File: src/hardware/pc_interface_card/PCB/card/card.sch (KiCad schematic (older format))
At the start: 16 parts, among them J1 USBC_IO_PWR, J2 USBC_PWR_ONLY, J3 10018784-10201TLF, J4 PD_I2C

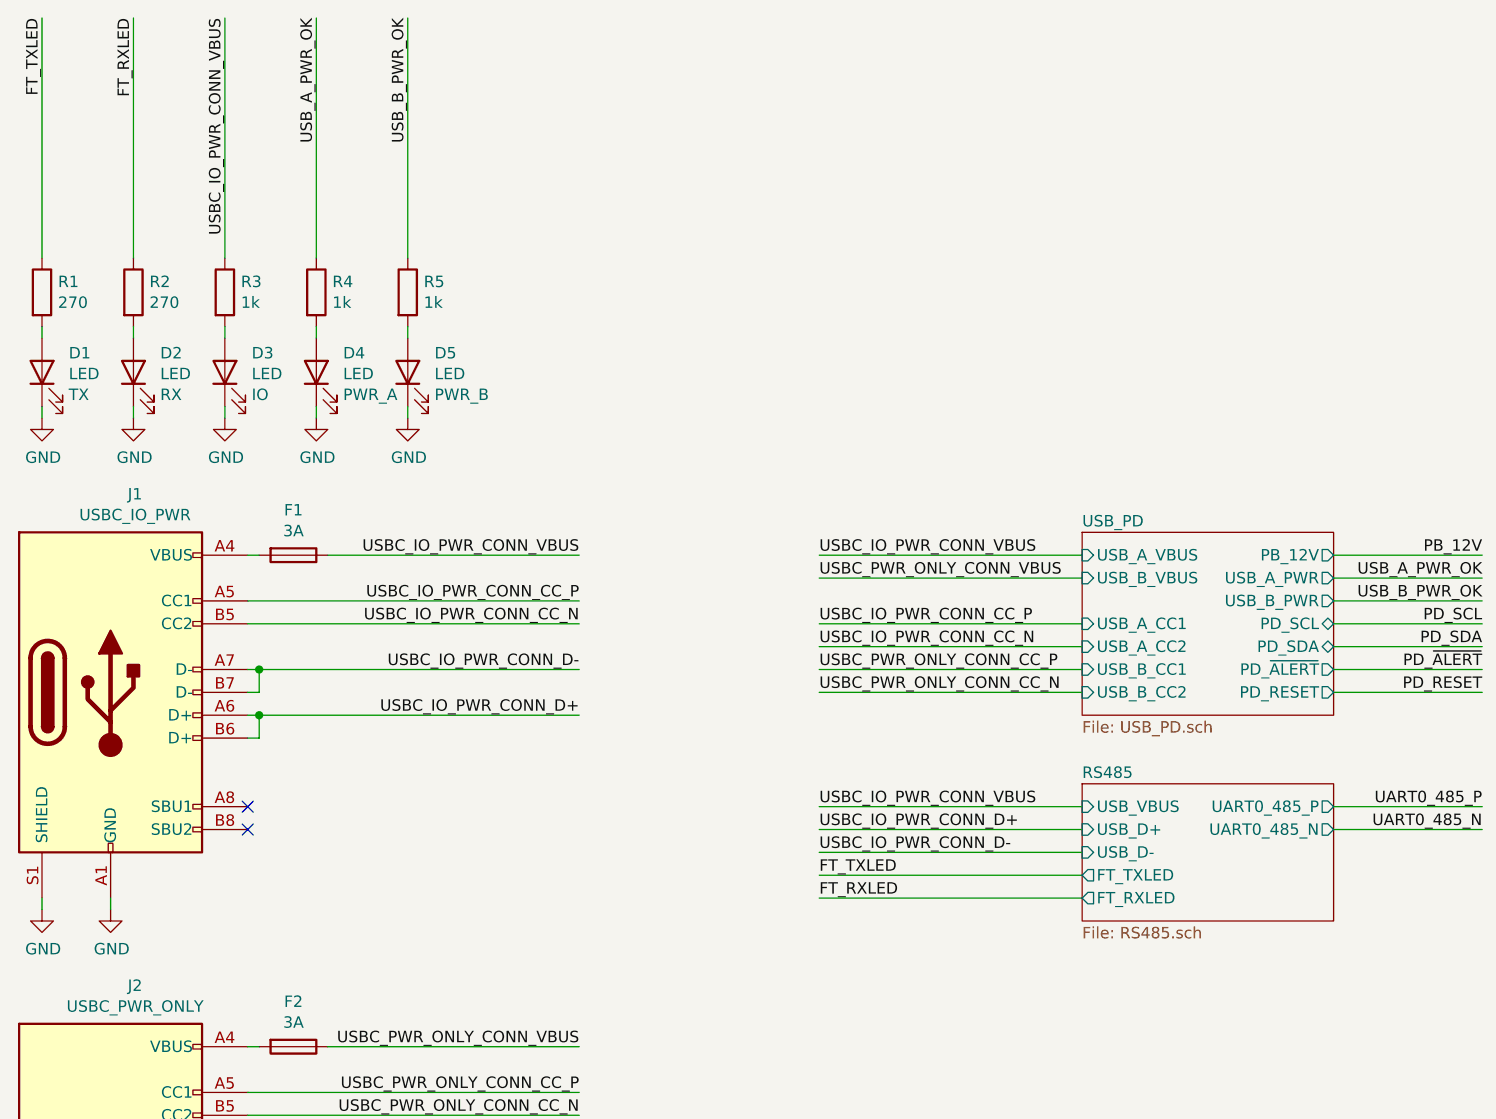
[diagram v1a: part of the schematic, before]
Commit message: Fixing RXLED and TXLED polarization
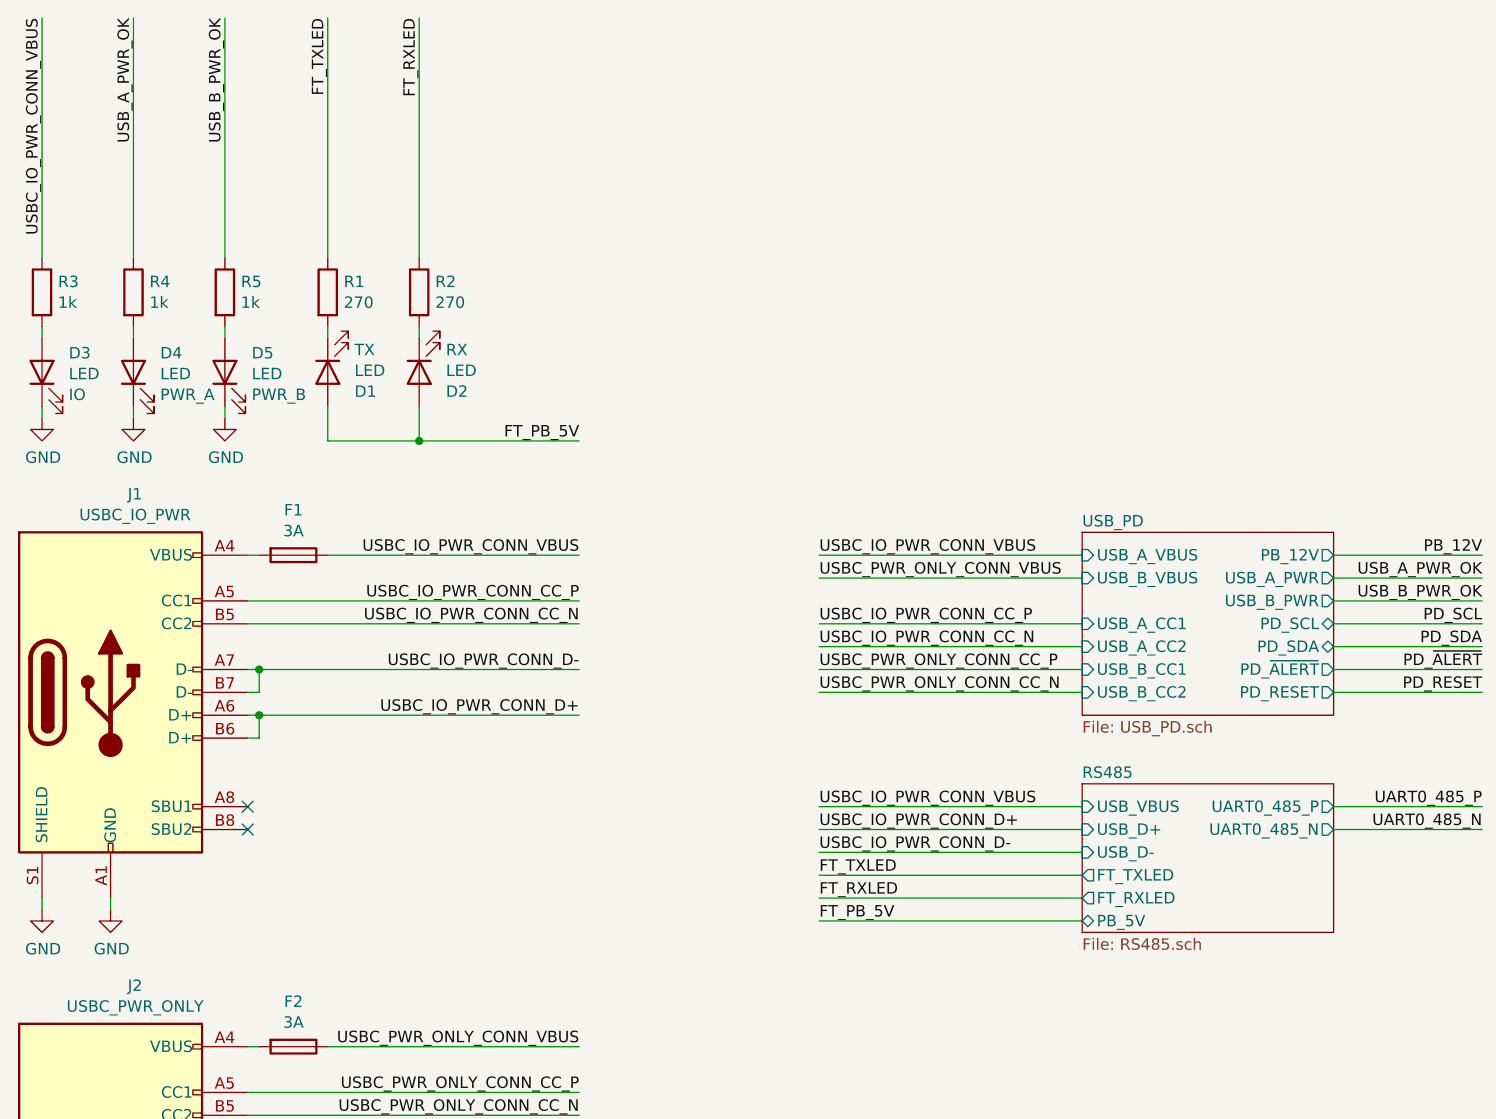
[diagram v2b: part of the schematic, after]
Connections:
- net GND: no longer D1.1 (K), D2.1 (K)
- net at R1.2: now also D1.1 (K); no longer D1.2 (A)
- net at R2.2: now also D2.1 (K); no longer D2.2 (A)
- new net FT_PB_5V: D1.2 (A), D2.2 (A)
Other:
- moved on the sheet: D1, D2, D3, D4, D5, R1, R2, R3, R4, R5
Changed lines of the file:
@@
 	8100 1850 8650 1850
-$Comp
-L Device:LED D1
-U 1 1 5E969A63
-P 1000 2150
-F 0 "D1" V 1084 2033 50  0000 R CNN
-F 1 "LED" V 993 2033 50  0000 R CNN
-F 2 "LED_THT:LED_D3.0mm" H 1000 2150 50  0001 C CNN
-F 3 "~" H 1000 2150 50  0001 C CNN
-F 4 "TX" V 902 2033 50  0000 R CNN "Info"
-	1    1000 2150
-	0    -1   -1   0
-$EndComp
 $Comp
 L Device:R R1
 U 1 1 5E96B671
-P 1000 1800
-F 0 "R1" H 1070 1846 50  0000 L CNN
-F 1 "270" H 1070 1755 50  0000 L CNN
-F 2 "Resistor_SMD:R_0603_1608Metric" V 930 1800 50  0001 C CNN
-F 3 "~" H 1000 1800 50  0001 C CNN
-	1    1000 1800
-	1    0    0    -1
-$EndComp
-$Comp
-L power:GND #PWR01
-U 1 1 5E970CD5
-P 1000 2350
-F 0 "#PWR01" H 1000 2100 50  0001 C CNN
-F 1 "GND" H 1005 2177 50  0000 C CNN
-F 2 "" H 1000 2350 50  0001 C CNN
-F 3 "" H 1000 2350 50  0001 C CNN
-	1    1000 2350
-	1    0    0    -1
-$EndComp
-Wire Wire Line
-	1000 2300 1000 2350
-Wire Wire Line
-	1000 1950 1000 2000
+P 2250 1800
+F 0 "R1" H 2320 1846 50  0000 L CNN
+F 1 "270" H 2320 1755 50  0000 L CNN
+F 2 "Resistor_SMD:R_0603_1608Metric" V 2180 1800 50  0001 C CNN
+F 3 "~" H 2250 1800 50  0001 C CNN
+	1    2250 1800
+	1    0    0    -1
+$EndComp
+Wire Wire Line
+	2250 1950 2250 2000
 $Comp
 L Device:LED D2
 U 1 1 5E97516D
-P 1400 2150
-F 0 "D2" V 1484 2033 50  0000 R CNN
-F 1 "LED" V 1393 2033 50  0000 R CNN
-F 2 "LED_THT:LED_D3.0mm" H 1400 2150 50  0001 C CNN
-F 3 "~" H 1400 2150 50  0001 C CNN
-F 4 "RX" V 1302 2033 50  0000 R CNN "Info"
-	1    1400 2150
-	0    -1   -1   0
+P 2650 2150
+F 0 "D2" V 2734 2033 50  0000 R CNN
+F 1 "LED" V 2643 2033 50  0000 R CNN
+F 2 "LED_THT:LED_D3.0mm" H 2650 2150 50  0001 C CNN
+F 3 "~" H 2650 2150 50  0001 C CNN
+F 4 "RX" V 2552 2033 50  0000 R CNN "Info"
+	1    2650 2150
+	0    -1   1    0
 $EndComp
 $Comp
 L Device:R R2
 U 1 1 5E975177
-P 1400 1800
-F 0 "R2" H 1470 1846 50  0000 L CNN
-F 1 "270" H 1470 1755 50  0000 L CNN
-F 2 "Resistor_SMD:R_0603_1608Metric" V 1330 1800 50  0001 C CNN
-F 3 "~" H 1400 1800 50  0001 C CNN
-	1    1400 1800
-	1    0    0    -1
-$EndComp
-$Comp
-L power:GND #PWR06
-U 1 1 5E975181
-P 1400 2350
-F 0 "#PWR06" H 1400 2100 50  0001 C CNN
-F 1 "GND" H 1405 2177 50  0000 C CNN
-F 2 "" H 1400 2350 50  0001 C CNN
-F 3 "" H 1400 2350 50  0001 C CNN
-	1    1400 2350
-	1    0    0    -1
-$EndComp
-Wire Wire Line
-	1400 2300 1400 2350
-Wire Wire Line
-	1400 1950 1400 2000
-Text Label 1000 600  3    50   ~ 0
+P 2650 1800
+F 0 "R2" H 2720 1846 50  0000 L CNN
+F 1 "270" H 2720 1755 50  0000 L CNN
+F 2 "Resistor_SMD:R_0603_1608Metric" V 2580 1800 50  0001 C CNN
+F 3 "~" H 2650 1800 50  0001 C CNN
+	1    2650 1800
+	1    0    0    -1
+$EndComp
+Wire Wire Line
+	2650 1950 2650 2000
+Text Label 2250 600  3    50   ~ 0
 FT_TXLED
-Text Label 1400 600  3    50   ~ 0
+Text Label 2650 600  3    50   ~ 0
 FT_RXLED
 Wire Wire Line
-	1400 600  1400 1650
-Wire Wire Line
-	1000 600  1000 1650
+	2650 600  2650 1650
+Wire Wire Line
+	2250 600  2250 1650
 Text Label 3350 3650 2    50   ~ 0
 USBC_IO_PWR_CONN_D+
@@
 	3350 5100 2250 5100
 $Sheet
-S 5550 3950 1100 600
+S 5550 3950 1100 650
 U 5EA5E705
 F0 "RS485" 50
@@
 F7 "USB_D-" I L 5550 4250 50
 F8 "USB_D+" I L 5550 4150 50
+F9 "PB_5V" B L 5550 4550 50
 $EndSheet
 Text Label 7300 4050 2    50   ~ 0
@@
 L Device:LED D3
 U 1 1 5E9B3E6F
-P 1800 2150
-F 0 "D3" V 1884 2033 50  0000 R CNN
-F 1 "LED" V 1793 2033 50  0000 R CNN
-F 2 "LED_THT:LED_D3.0mm" H 1800 2150 50  0001 C CNN
-F 3 "~" H 1800 2150 50  0001 C CNN
-F 4 "IO" V 1702 2033 50  0000 R CNN "Info"
-	1    1800 2150
+P 1000 2150
+F 0 "D3" V 1084 2033 50  0000 R CNN
+F 1 "LED" V 993 2033 50  0000 R CNN
+F 2 "LED_THT:LED_D3.0mm" H 1000 2150 50  0001 C CNN
+F 3 "~" H 1000 2150 50  0001 C CNN
+F 4 "IO" V 902 2033 50  0000 R CNN "Info"
+	1    1000 2150
 	0    -1   -1   0
 $EndComp
@@
 L Device:R R3
 U 1 1 5E9B3E79
-P 1800 1800
-F 0 "R3" H 1870 1846 50  0000 L CNN
-F 1 "1k" H 1870 1755 50  0000 L CNN
-F 2 "Resistor_SMD:R_0603_1608Metric" V 1730 1800 50  0001 C CNN
-F 3 "~" H 1800 1800 50  0001 C CNN
-	1    1800 1800
+P 1000 1800
+F 0 "R3" H 1070 1846 50  0000 L CNN
+F 1 "1k" H 1070 1755 50  0000 L CNN
+F 2 "Resistor_SMD:R_0603_1608Metric" V 930 1800 50  0001 C CNN
+F 3 "~" H 1000 1800 50  0001 C CNN
+	1    1000 1800
 	1    0    0    -1
 $EndComp
@@
 L power:GND #PWR07
 U 1 1 5E9B3E83
-P 1800 2350
-F 0 "#PWR07" H 1800 2100 50  0001 C CNN
-F 1 "GND" H 1805 2177 50  0000 C CNN
-F 2 "" H 1800 2350 50  0001 C CNN
-F 3 "" H 1800 2350 50  0001 C CNN
-	1    1800 2350
-	1    0    0    -1
-$EndComp
-Wire Wire Line
-	1800 2300 1800 2350
-Wire Wire Line
-	1800 1950 1800 2000
+P 1000 2350
+F 0 "#PWR07" H 1000 2100 50  0001 C CNN
+F 1 "GND" H 1005 2177 50  0000 C CNN
+F 2 "" H 1000 2350 50  0001 C CNN
+F 3 "" H 1000 2350 50  0001 C CNN
+	1    1000 2350
+	1    0    0    -1
+$EndComp
+Wire Wire Line
+	1000 2300 1000 2350
+Wire Wire Line
+	1000 1950 1000 2000
 $Comp
 L Device:LED D4
 U 1 1 5E9B3E90
-P 2200 2150
-F 0 "D4" V 2284 2033 50  0000 R CNN
-F 1 "LED" V 2193 2033 50  0000 R CNN
-F 2 "LED_THT:LED_D3.0mm" H 2200 2150 50  0001 C CNN
-F 3 "~" H 2200 2150 50  0001 C CNN
-F 4 "PWR_A" V 2102 2033 50  0000 R CNN "Info"
-	1    2200 2150
+P 1400 2150
+F 0 "D4" V 1484 2033 50  0000 R CNN
+F 1 "LED" V 1393 2033 50  0000 R CNN
+F 2 "LED_THT:LED_D3.0mm" H 1400 2150 50  0001 C CNN
+F 3 "~" H 1400 2150 50  0001 C CNN
+F 4 "PWR_A" V 1302 2033 50  0000 R CNN "Info"
+	1    1400 2150
 	0    -1   -1   0
 $EndComp
@@
 L Device:R R4
 U 1 1 5E9B3E9A
-P 2200 1800
-F 0 "R4" H 2270 1846 50  0000 L CNN
-F 1 "1k" H 2270 1755 50  0000 L CNN
-F 2 "Resistor_SMD:R_0603_1608Metric" V 2130 1800 50  0001 C CNN
-F 3 "~" H 2200 1800 50  0001 C CNN
-	1    2200 1800
+P 1400 1800
+F 0 "R4" H 1470 1846 50  0000 L CNN
+F 1 "1k" H 1470 1755 50  0000 L CNN
+F 2 "Resistor_SMD:R_0603_1608Metric" V 1330 1800 50  0001 C CNN
+F 3 "~" H 1400 1800 50  0001 C CNN
+	1    1400 1800
 	1    0    0    -1
 $EndComp
@@
 L power:GND #PWR08
 U 1 1 5E9B3EA4
-P 2200 2350
-F 0 "#PWR08" H 2200 2100 50  0001 C CNN
-F 1 "GND" H 2205 2177 50  0000 C CNN
-F 2 "" H 2200 2350 50  0001 C CNN
-F 3 "" H 2200 2350 50  0001 C CNN
-	1    2200 2350
-	1    0    0    -1
-$EndComp
-Wire Wire Line
-	2200 2300 2200 2350
-Wire Wire Line
-	2200 1950 2200 2000
-Wire Wire Line
-	2200 600  2200 1650
-Wire Wire Line
-	1800 600  1800 1650
+P 1400 2350
+F 0 "#PWR08" H 1400 2100 50  0001 C CNN
+F 1 "GND" H 1405 2177 50  0000 C CNN
+F 2 "" H 1400 2350 50  0001 C CNN
+F 3 "" H 1400 2350 50  0001 C CNN
+	1    1400 2350
+	1    0    0    -1
+$EndComp
+Wire Wire Line
+	1400 2300 1400 2350
+Wire Wire Line
+	1400 1950 1400 2000
+Wire Wire Line
+	1400 600  1400 1650
+Wire Wire Line
+	1000 600  1000 1650
 Text Label 7300 3050 2    50   ~ 0
 USB_A_PWR_OK
@@
 Wire Wire Line
 	6650 3150 7300 3150
-Text Label 2200 600  3    50   ~ 0
+Text Label 1400 600  3    50   ~ 0
 USB_A_PWR_OK
 $Sheet
@@
 L Device:LED D5
 U 1 1 5EA3750F
-P 2600 2150
-F 0 "D5" V 2684 2033 50  0000 R CNN
-F 1 "LED" V 2593 2033 50  0000 R CNN
-F 2 "LED_THT:LED_D3.0mm" H 2600 2150 50  0001 C CNN
-F 3 "~" H 2600 2150 50  0001 C CNN
-F 4 "PWR_B" V 2502 2033 50  0000 R CNN "Info"
-	1    2600 2150
+P 1800 2150
+F 0 "D5" V 1884 2033 50  0000 R CNN
+F 1 "LED" V 1793 2033 50  0000 R CNN
+F 2 "LED_THT:LED_D3.0mm" H 1800 2150 50  0001 C CNN
+F 3 "~" H 1800 2150 50  0001 C CNN
+F 4 "PWR_B" V 1702 2033 50  0000 R CNN "Info"
+	1    1800 2150
 	0    -1   -1   0
 $EndComp
@@
 L Device:R R5
 U 1 1 5EA37519
-P 2600 1800
-F 0 "R5" H 2670 1846 50  0000 L CNN
-F 1 "1k" H 2670 1755 50  0000 L CNN
-F 2 "Resistor_SMD:R_0603_1608Metric" V 2530 1800 50  0001 C CNN
-F 3 "~" H 2600 1800 50  0001 C CNN
-	1    2600 1800
+P 1800 1800
+F 0 "R5" H 1870 1846 50  0000 L CNN
+F 1 "1k" H 1870 1755 50  0000 L CNN
+F 2 "Resistor_SMD:R_0603_1608Metric" V 1730 1800 50  0001 C CNN
+F 3 "~" H 1800 1800 50  0001 C CNN
+	1    1800 1800
 	1    0    0    -1
 $EndComp
@@
 L power:GND #PWR09
 U 1 1 5EA37523
-P 2600 2350
-F 0 "#PWR09" H 2600 2100 50  0001 C CNN
-F 1 "GND" H 2605 2177 50  0000 C CNN
-F 2 "" H 2600 2350 50  0001 C CNN
-F 3 "" H 2600 2350 50  0001 C CNN
-	1    2600 2350
-	1    0    0    -1
-$EndComp
-Wire Wire Line
-	2600 2300 2600 2350
-Wire Wire Line
-	2600 1950 2600 2000
-Wire Wire Line
-	2600 600  2600 1650
-Text Label 2600 600  3    50   ~ 0
+P 1800 2350
+F 0 "#PWR09" H 1800 2100 50  0001 C CNN
+F 1 "GND" H 1805 2177 50  0000 C CNN
+F 2 "" H 1800 2350 50  0001 C CNN
+F 3 "" H 1800 2350 50  0001 C CNN
+	1    1800 2350
+	1    0    0    -1
+$EndComp
+Wire Wire Line
+	1800 2300 1800 2350
+Wire Wire Line
+	1800 1950 1800 2000
+Wire Wire Line
+	1800 600  1800 1650
+Text Label 1800 600  3    50   ~ 0
 USB_B_PWR_OK
-Text Label 1800 600  3    50   ~ 0
+Text Label 1000 600  3    50   ~ 0
 USBC_IO_PWR_CONN_VBUS
 Text Label 3350 3150 2    50   ~ 0
@@
 Text Label 3350 5400 2    50   ~ 0
 USBC_PWR_ONLY_CONN_CC_N
+Text Label 4400 4550 0    50   ~ 0
+FT_PB_5V
+Wire Wire Line
+	4400 4550 5550 4550
+Text Label 3350 2450 2    50   ~ 0
+FT_PB_5V
+Wire Wire Line
+	3350 2450 2650 2450
+Wire Wire Line
+	2250 2300 2250 2450
+Wire Wire Line
+	2650 2300 2650 2450
+Connection ~ 2650 2450
+Wire Wire Line
+	2650 2450 2250 2450
+$Comp
+L Device:LED D1
+U 1 1 5E969A63
+P 2250 2150
+F 0 "D1" V 2334 2033 50  0000 R CNN
+F 1 "LED" V 2243 2033 50  0000 R CNN
+F 2 "LED_THT:LED_D3.0mm" H 2250 2150 50  0001 C CNN
+F 3 "~" H 2250 2150 50  0001 C CNN
+F 4 "TX" V 2152 2033 50  0000 R CNN "Info"
+	1    2250 2150
+	0    -1   1    0
+$EndComp
 $EndSCHEMATC

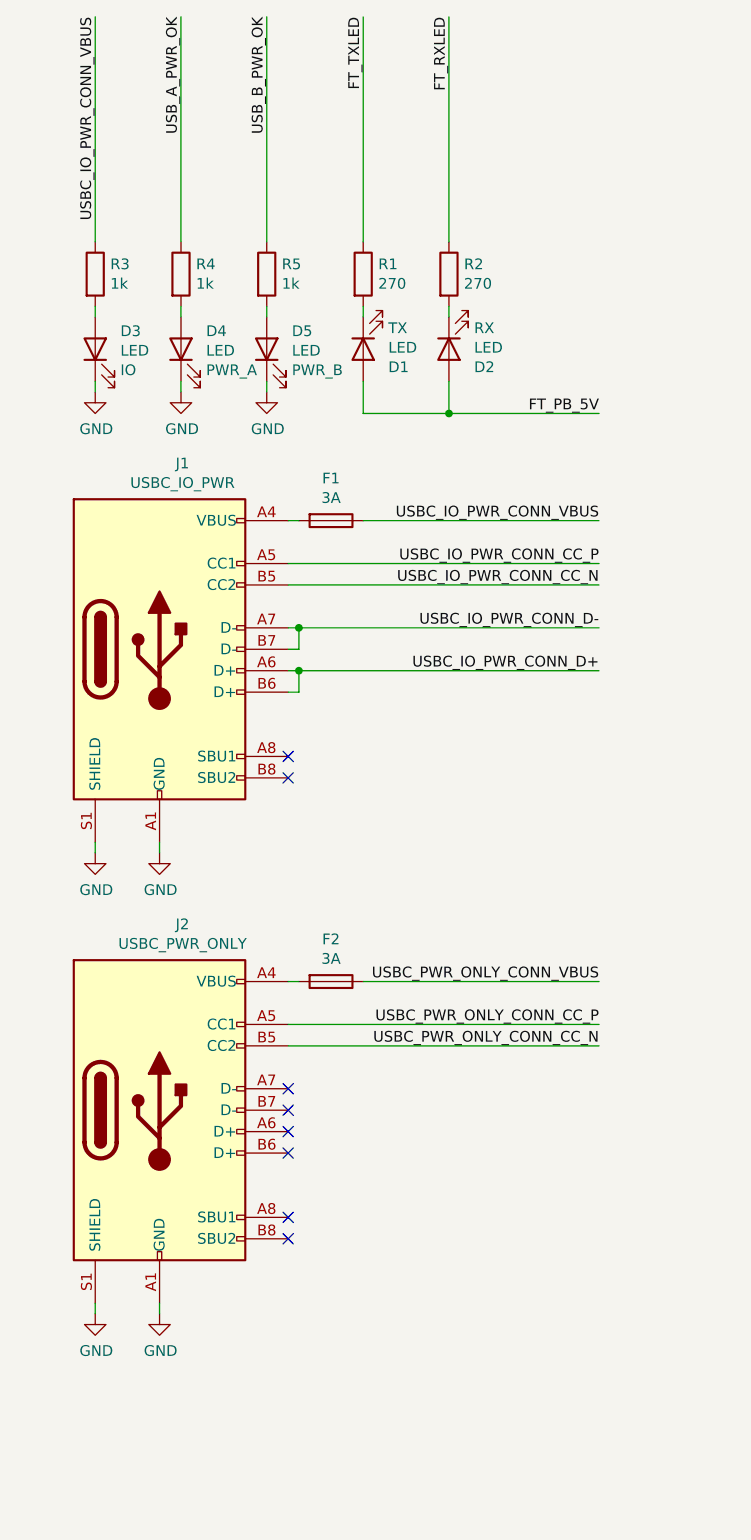
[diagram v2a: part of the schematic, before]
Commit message: adding barrel jack connector for powering PC interface card and mooving the status LEDs on the front panel
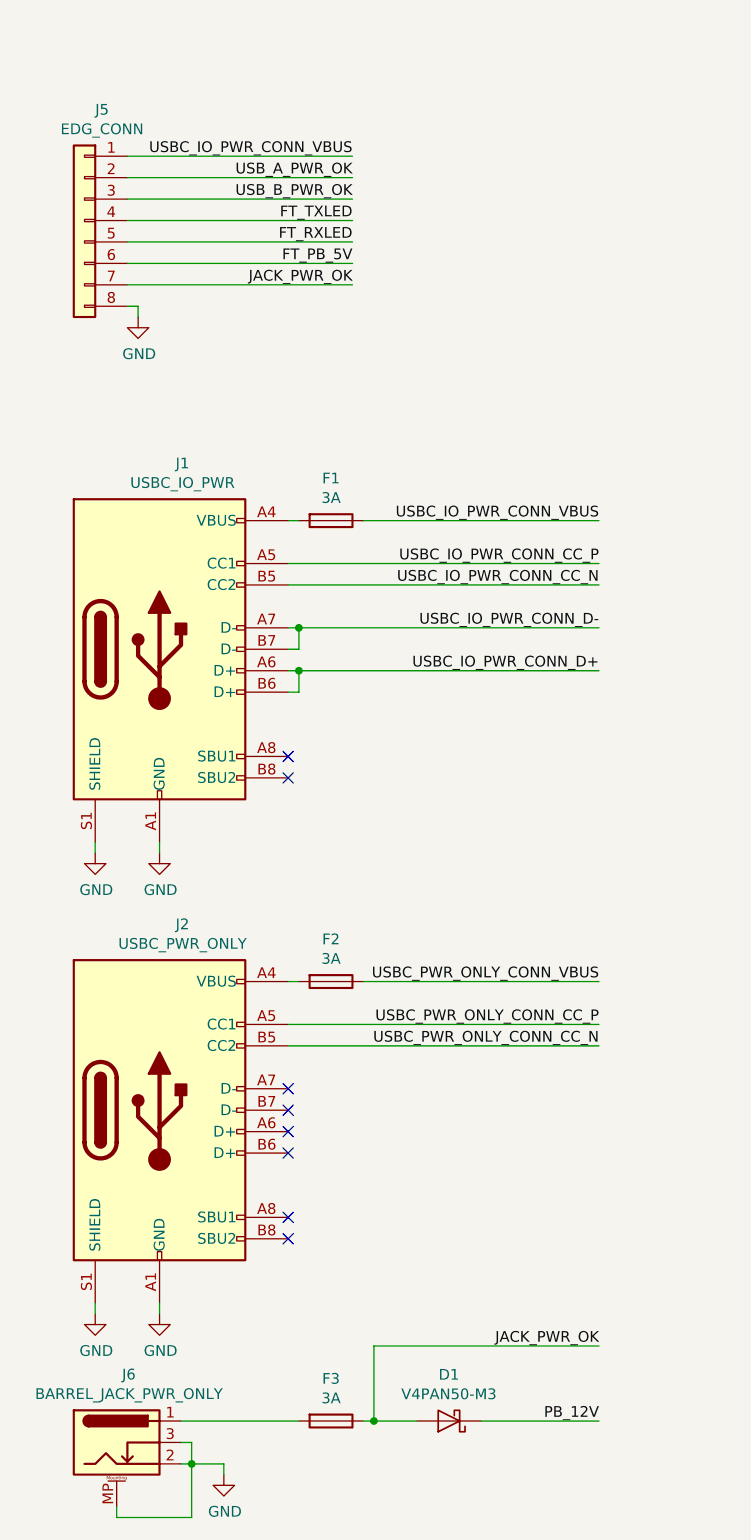
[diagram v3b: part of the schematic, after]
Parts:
- removed D1, D2, D3, D4, D5: LED, LED_THT:LED_D3.0mm, symbol Device:LED
- removed R1, R2: 270, Resistor_SMD:R_0603_1608Metric, symbol Device:R
- removed R3, R4, R5: 1k, Resistor_SMD:R_0603_1608Metric, symbol Device:R
- added D1: V4PAN50-M3, kicad-lib:SMPA, symbol Device:D_Schottky
- added F3: 3A, Fuse:Fuse_0603_1608Metric, symbol Device:Fuse
- added J5: EDG_CONN, Connector_PinSocket_2.54mm:PinSocket_1x08_P2.54mm_Vertical, symbol Connector_Generic:Conn_01x08
- added J6: BARREL_JACK_PWR_ONLY, kicad-lib:CUI_PJ-079BH, symbol Connector:Barrel_Jack_Switch_MountingPin
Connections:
- net FT_PB_5V: now also J5.6 (Pin_6)
- net FT_RXLED: now also J5.5 (Pin_5)
- net FT_TXLED: now also J5.4 (Pin_4)
- net GND: now also J5.8 (Pin_8), J6.2, J6.3, J6.MP (MountPin)
- net PB_12V: now also D1.1 (K)
- net USBC_IO_PWR_CONN_VBUS: now also J5.1 (Pin_1)
- net USB_A_PWR_OK: now also J5.2 (Pin_2)
- net USB_B_PWR_OK: now also J5.3 (Pin_3)
- new net: F3.2, J6.1
- new net JACK_PWR_OK: D1.2 (A), F3.1, J5.7 (Pin_7)
